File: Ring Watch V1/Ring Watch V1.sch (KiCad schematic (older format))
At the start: 13 parts, among them J1 Programming Header, J2 CR2023 Socket, U1 ATtiny85-20SU, U2 PCF8523T, Y1 32.768

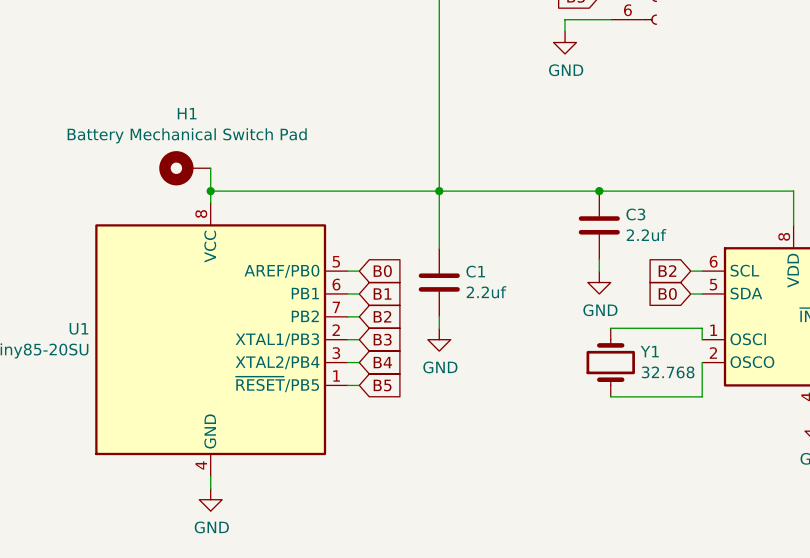
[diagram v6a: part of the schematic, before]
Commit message: added i2c pullups
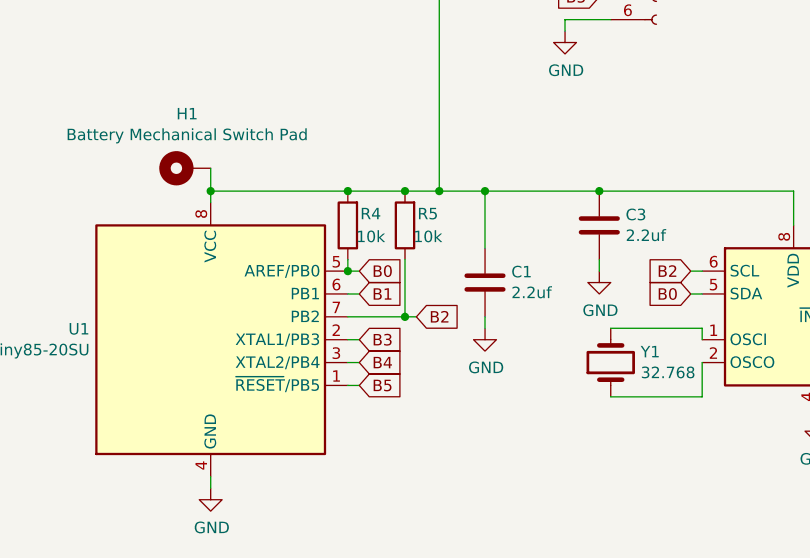
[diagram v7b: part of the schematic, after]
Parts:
- added R4, R5: 10k, Resistor_SMD:R_0805_2012Metric_Pad1.15x1.40mm_HandSolder, symbol Device:R
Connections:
- net B0: now also R4.1
- net B2: now also R5.1
- net at C1.1, C3.1, H1.1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: now also R4.2, R5.2
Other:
- moved on the sheet: C1
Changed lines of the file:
@@
 L Device:C C1
 U 1 1 5FBC4359
-P 3100 2650
-F 0 "C1" H 3215 2696 50  0000 L CNN
-F 1 "2.2uf" H 3215 2605 50  0000 L CNN
-F 2 "Capacitor_SMD:C_0805_2012Metric_Pad1.15x1.40mm_HandSolder" H 3138 2500 50  0001 C CNN
-F 3 "~" H 3100 2650 50  0001 C CNN
-	1    3100 2650
+P 3300 2650
+F 0 "C1" H 3415 2696 50  0000 L CNN
+F 1 "2.2uf" H 3415 2605 50  0000 L CNN
+F 2 "Capacitor_SMD:C_0805_2012Metric_Pad1.15x1.40mm_HandSolder" H 3338 2500 50  0001 C CNN
+F 3 "~" H 3300 2650 50  0001 C CNN
+	1    3300 2650
 	1    0    0    -1
 $EndComp
@@
 L power:GND #PWR0101
 U 1 1 5FBC4E8A
-P 3100 2850
-F 0 "#PWR0101" H 3100 2600 50  0001 C CNN
-F 1 "GND" H 3105 2677 50  0000 C CNN
-F 2 "" H 3100 2850 50  0001 C CNN
-F 3 "" H 3100 2850 50  0001 C CNN
-	1    3100 2850
-	1    0    0    -1
-$EndComp
-Wire Wire Line
-	3100 2800 3100 2850
+P 3300 2850
+F 0 "#PWR0101" H 3300 2600 50  0001 C CNN
+F 1 "GND" H 3305 2677 50  0000 C CNN
+F 2 "" H 3300 2850 50  0001 C CNN
+F 3 "" H 3300 2850 50  0001 C CNN
+	1    3300 2850
+	1    0    0    -1
+$EndComp
 $Comp
 L power:+BATT #PWR0103
@@
 Wire Wire Line
 	2100 3500 2100 3550
-Text GLabel 2750 2800 2    50   Input ~ 0
-B2
-Wire Wire Line
-	2700 2800 2750 2800
-Text GLabel 2750 2600 2    50   Input ~ 0
-B0
-Wire Wire Line
-	2700 2600 2750 2600
 Text GLabel 4200 2700 0    50   Input ~ 0
 B0
@@
 	6100 2950 6150 2950
 Wire Wire Line
-	2100 2250 3100 2250
-Wire Wire Line
-	3100 2250 3100 2500
+	2100 2250 2700 2250
 Connection ~ 2100 2250
 Wire Wire Line
@@
 	3100 1000 3100 2250
 Wire Wire Line
-	3100 2250 3800 2250
-Wire Wire Line
 	4650 2250 4650 2400
 $Comp
@@
 Wire Wire Line
 	3800 2550 3800 2600
+Wire Wire Line
+	2700 2600 2750 2600
+Text GLabel 3000 2800 2    50   Input ~ 0
+B2
+Text GLabel 2750 2600 2    50   Input ~ 0
+B0
+Wire Wire Line
+	3100 2250 3300 2250
+$Comp
+L Device:R R4
+U 1 1 5FEE9CD3
+P 2700 2400
+F 0 "R4" H 2600 2350 50  0000 C CNN
+F 1 "10k" H 2600 2450 50  0000 C CNN
+F 2 "Resistor_SMD:R_0805_2012Metric_Pad1.15x1.40mm_HandSolder" V 2630 2400 50  0001 C CNN
+F 3 "~" H 2700 2400 50  0001 C CNN
+	1    2700 2400
+	-1   0    0    1
+$EndComp
+$Comp
+L Device:R R5
+U 1 1 5FEEAE89
+P 2950 2400
+F 0 "R5" H 2850 2350 50  0000 C CNN
+F 1 "10k" H 2850 2450 50  0000 C CNN
+F 2 "Resistor_SMD:R_0805_2012Metric_Pad1.15x1.40mm_HandSolder" V 2880 2400 50  0001 C CNN
+F 3 "~" H 2950 2400 50  0001 C CNN
+	1    2950 2400
+	-1   0    0    1
+$EndComp
+Connection ~ 2950 2250
+Wire Wire Line
+	2950 2250 3100 2250
+Connection ~ 2700 2250
+Wire Wire Line
+	2700 2250 2950 2250
+Wire Wire Line
+	2700 2550 2700 2600
+Connection ~ 2700 2600
+Wire Wire Line
+	3300 2500 3300 2250
+Connection ~ 3300 2250
+Wire Wire Line
+	3300 2250 3800 2250
+Wire Wire Line
+	3300 2800 3300 2850
+Wire Wire Line
+	2700 2800 2950 2800
+Wire Wire Line
+	2950 2550 2950 2800
+Connection ~ 2950 2800
+Wire Wire Line
+	2950 2800 3000 2800
 $EndSCHEMATC

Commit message: changed crystal footprint, added preliminary BOMs
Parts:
- Y1: footprint Crystal:Crystal_SMD_Abracon_ABM7-2Pin_6.0x3.5mm -> Crystal:Crystal_SMD_3215-2Pin_3.2x1.5mm
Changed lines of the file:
@@
 F 0 "Y1" V 3896 2869 50  0000 R CNN
 F 1 "32.768" V 3805 2869 50  0000 R CNN
-F 2 "Crystal:Crystal_SMD_Abracon_ABM7-2Pin_6.0x3.5mm" H 3850 3000 50  0001 C CNN
+F 2 "Crystal:Crystal_SMD_3215-2Pin_3.2x1.5mm" H 3850 3000 50  0001 C CNN
 F 3 "~" H 3850 3000 50  0001 C CNN
 	1    3850 3000
